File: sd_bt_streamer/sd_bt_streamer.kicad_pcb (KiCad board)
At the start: 2 copper layers, 58.3 x 46 mm, 7 parts, among them J1 Micro_SD_Card_Det, U1 SD_MMC_FOOTPRINT, U2 nRF52-Bluefruit

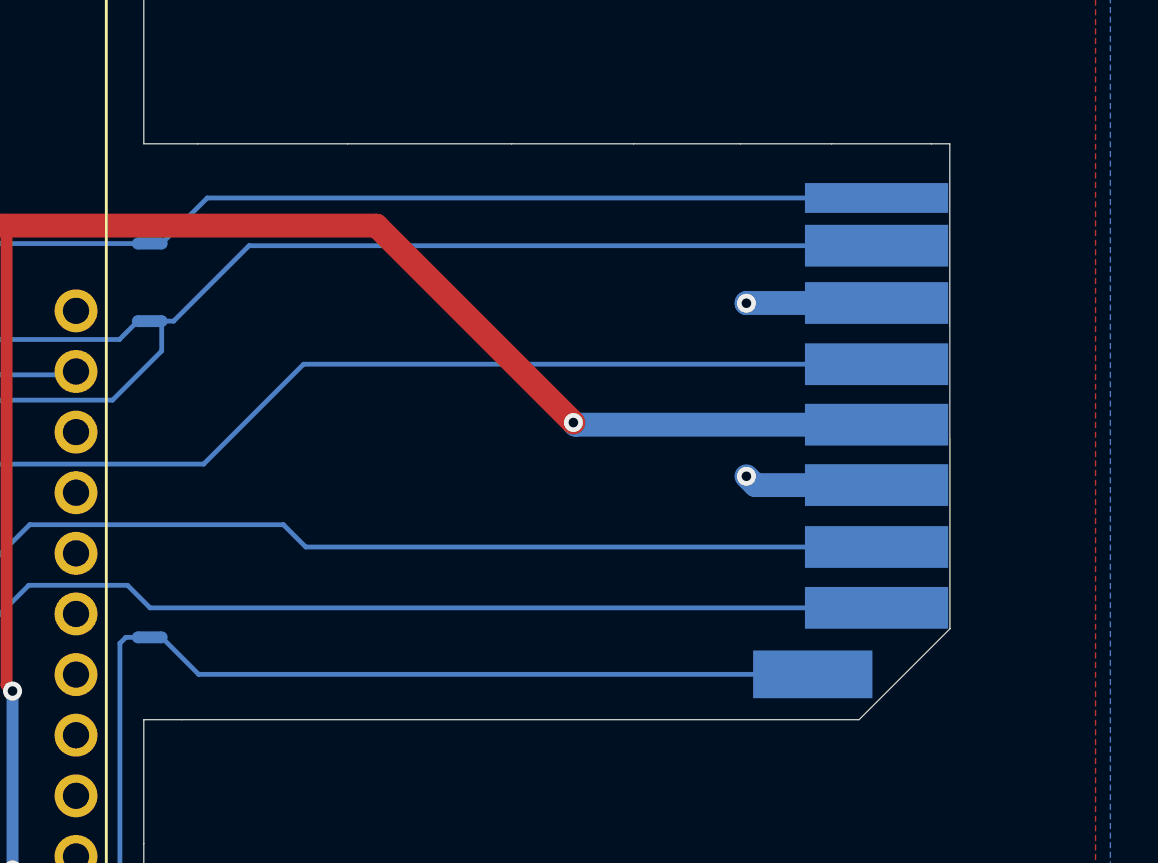
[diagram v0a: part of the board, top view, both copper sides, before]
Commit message: extended SD card by 5mm
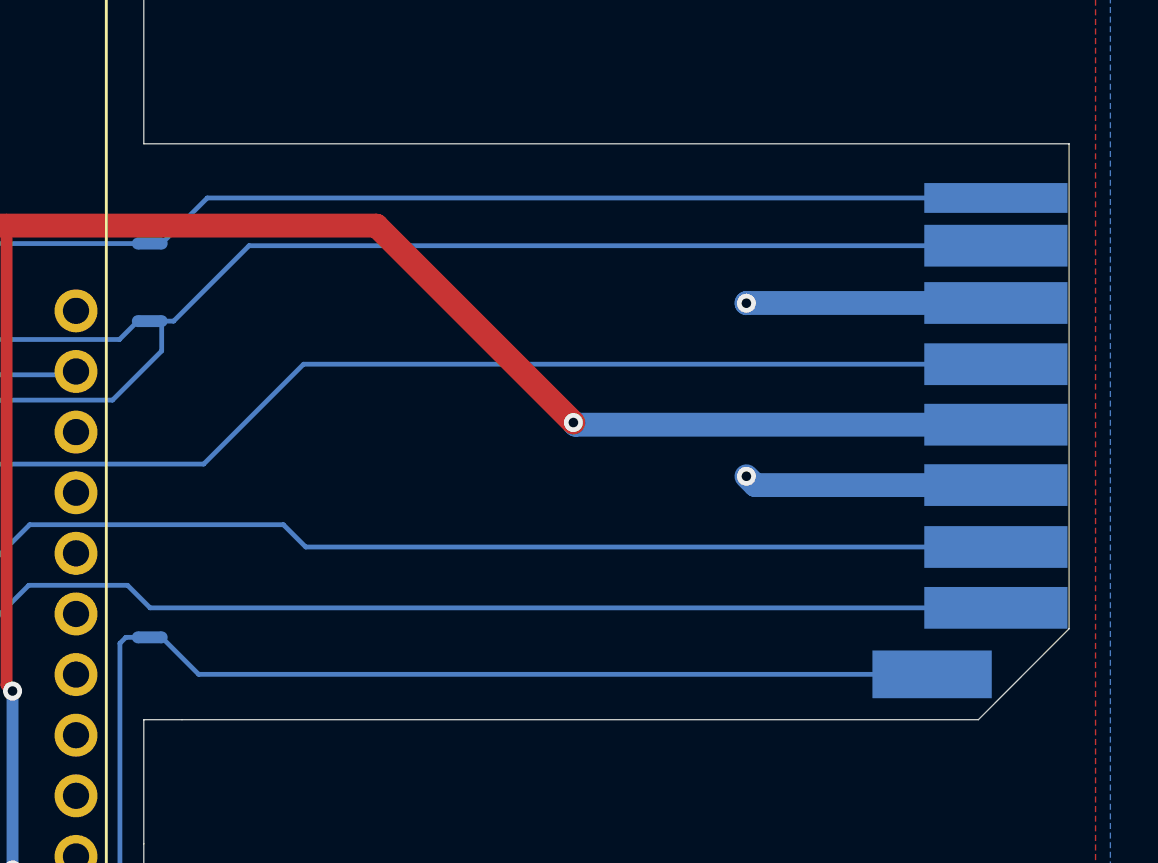
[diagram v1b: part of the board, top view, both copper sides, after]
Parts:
- moved U1 5.00 mm to (198.0, 81.5)
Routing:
- net GND: track 14.3 -> 24.3 mm
- net /MOSI: track 77.4 -> 82.4 mm
- net /MISO: track 67.9 -> 72.9 mm
- net /DAT2_T: track 27.9 -> 32.9 mm
- net /CS: track 75.3 -> 80.3 mm
- net /CLK: track 76.9 -> 81.9 mm
- net +3V3: track 101.8 -> 106.8 mm
- net /DAT1_T: track 30.7 -> 35.7 mm
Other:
- board size 58.3 x 46 mm -> 63.3 x 46 mm
